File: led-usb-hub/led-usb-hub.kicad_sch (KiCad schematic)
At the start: 136 parts, among them J1 USBC_USB2.0, J2 RGBUSB_54-00266, J3 RGBUSB_54-00266, J4 RGBUSB_54-00266, J5 SWD, SW1 RESET, SW2 BOOLSEL, SW3 LED_EN, U1 RP2040, U10 TPD2EUSB30, U11 TPD2EUSB30, U12 TC54VN3002, U13 W25Q16JVSN, U2 TPS2042D, U3 TPS2042D, U4 TPS563257DRLR, U5 TPS563257DRLR, U6 TUSB2046IBVF, U7 TPD2EUSB30, U8 TPD2EUSB30, U9 TPD2EUSB30, Y1 12Mhz, Y2 6Mhz

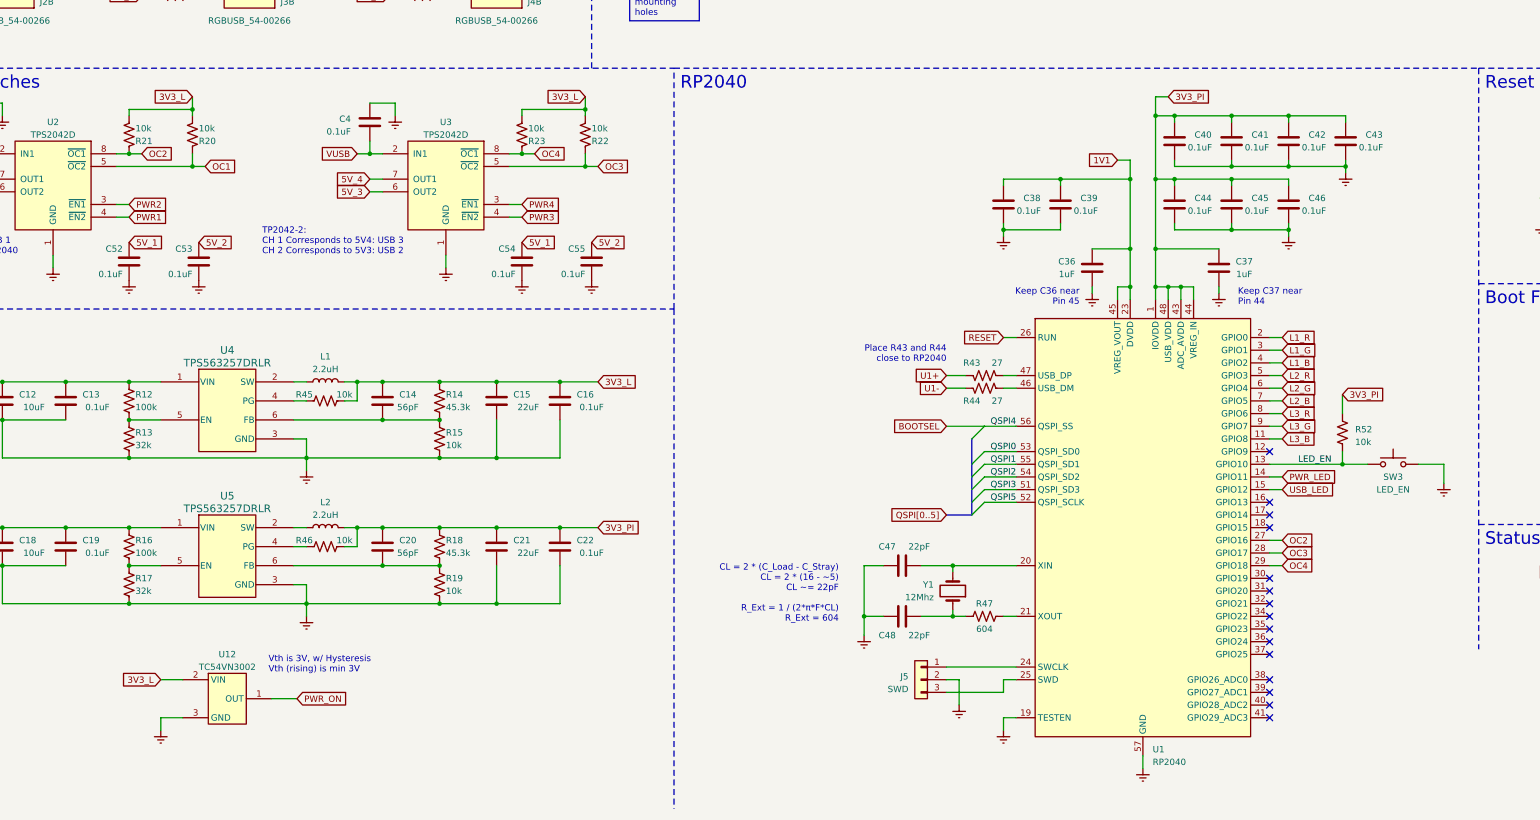
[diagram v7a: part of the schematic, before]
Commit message: Fix decoupling cap count and start component arrangement
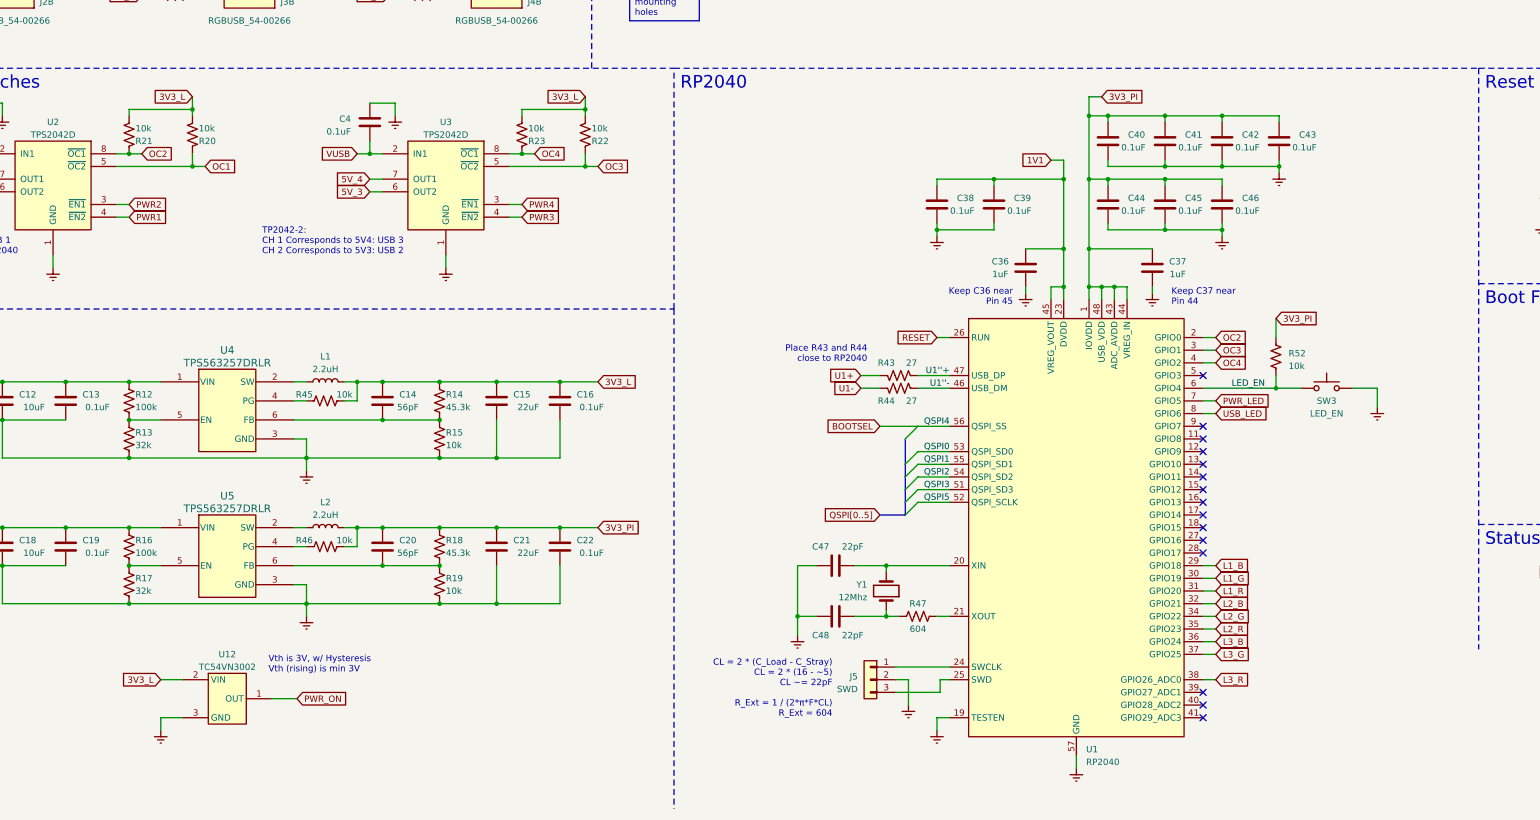
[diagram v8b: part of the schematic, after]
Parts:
- removed C52, C53, C54, C55: 0.1uF, Capacitor_SMD:C_0603_1608Metric_Pad1.08x0.95mm_HandSolder, symbol Device:C
- U10, U11, U7, U8, U9: footprint DRT0003A -> TPD2EUSB30DRTR:DRT0003A
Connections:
- net L1_B: now also U1.29 (GPIO18); no longer U1.4 (GPIO2)
- net L1_G: now also U1.30 (GPIO19); no longer U1.3 (GPIO1)
- net L1_R: now also U1.31 (GPIO20); no longer U1.2 (GPIO0)
- net L2_B: now also U1.32 (GPIO21); no longer U1.7 (GPIO5)
- net L2_G: now also U1.34 (GPIO22); no longer U1.6 (GPIO4)
- net L2_R: now also U1.35 (GPIO23); no longer U1.5 (GPIO3)
- net L3_B: now also U1.36 (GPIO24); no longer U1.11 (GPIO8)
- net L3_G: now also U1.37 (GPIO25); no longer U1.9 (GPIO7)
- net L3_R: now also U1.38 (GPIO26_ADC0); no longer U1.8 (GPIO6)
- net LED_EN: now also U1.6 (GPIO4); no longer U1.13 (GPIO10)
- net OC2: now also U1.2 (GPIO0); no longer U1.27 (GPIO16)
- net OC3: now also U1.3 (GPIO1); no longer U1.28 (GPIO17)
- net OC4: now also U1.4 (GPIO2); no longer U1.29 (GPIO18)
- net PWR_LED: now also U1.7 (GPIO5); no longer U1.14 (GPIO11)
- net USB_LED: now also U1.8 (GPIO6); no longer U1.15 (GPIO12)
- net U1''+: now reaches R43.2, U1.47 (USB_DP)
- net U1''-: now reaches R44.2, U1.46 (USB_DM)
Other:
- moved on the sheet: C36, C37, C38, C39, C40, C41, C42, C43, C44, C45, C46, C47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
